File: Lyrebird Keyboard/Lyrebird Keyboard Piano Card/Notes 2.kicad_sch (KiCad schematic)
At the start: 80 parts, among them IC21 CD4024BE, IC22 CD4024BE, IC23 CD4024BE, IC24 CD4024BE, IC25 CD4024BE, IC26 CD4024BE

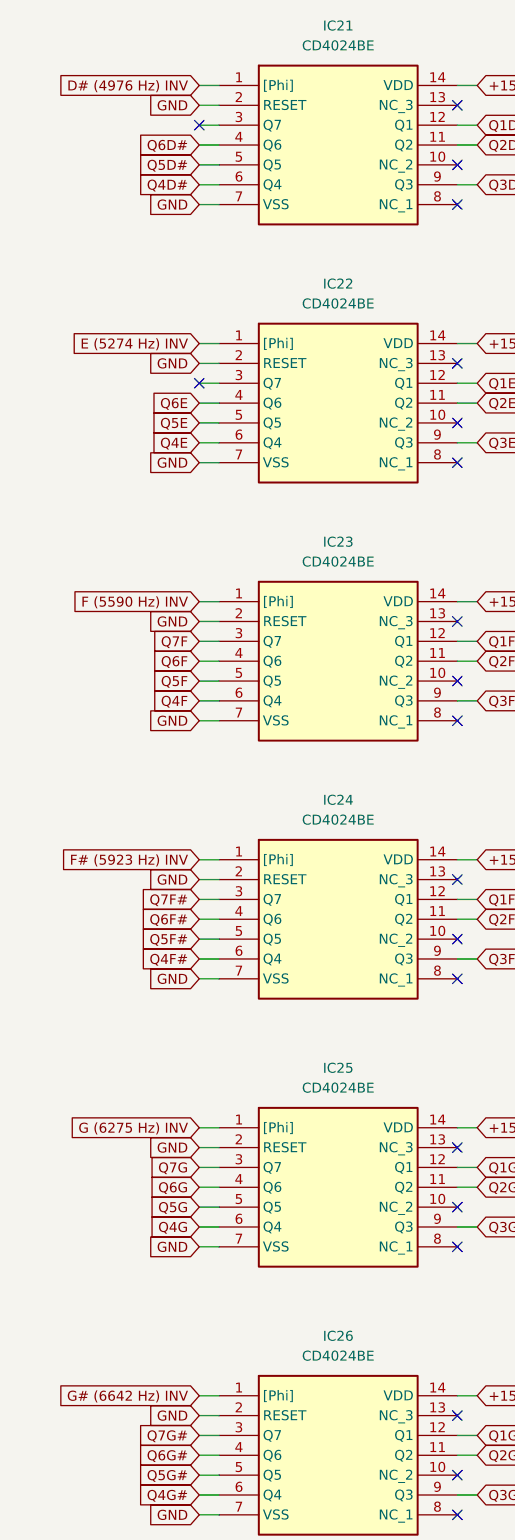
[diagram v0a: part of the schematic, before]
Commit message: Piano Board Layout
Started doing circuit that creates the piano sound.
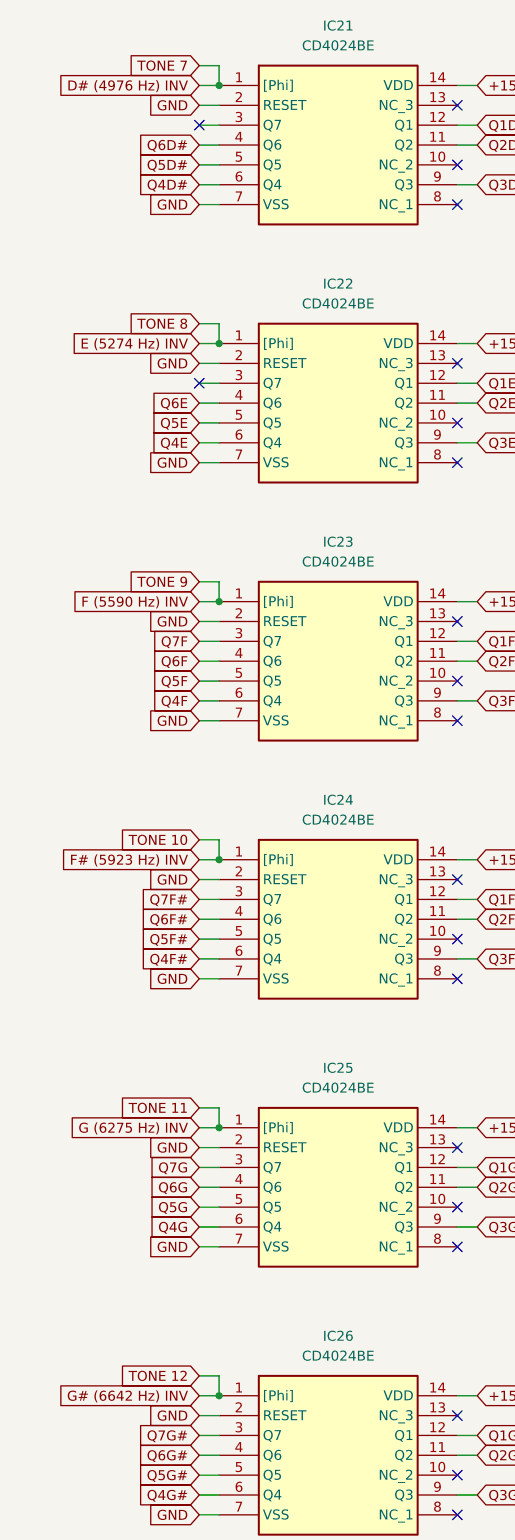
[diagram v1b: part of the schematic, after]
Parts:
- IC21, IC22, IC23, IC24, IC25, IC26: footprint DIP794W53P254L1930H508Q14N -> SamacSys_Parts:DIP794W53P254L1930H508Q14N
